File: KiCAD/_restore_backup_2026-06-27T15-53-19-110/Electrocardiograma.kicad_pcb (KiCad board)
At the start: 2 copper layers, 56.5 x 56.9 mm, 63 parts, among them J1 54-00174, J2 Conn_01x02_Pin, J4 Conn_01x02_Pin, J5 Conn_01x02_Pin, J6 Conn_01x04_Pin, U1 INA823DT, U2 ESP32-C3-WROOM-02, U3 TLV1117-33, U4 TLV4888, U5 TLV4888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

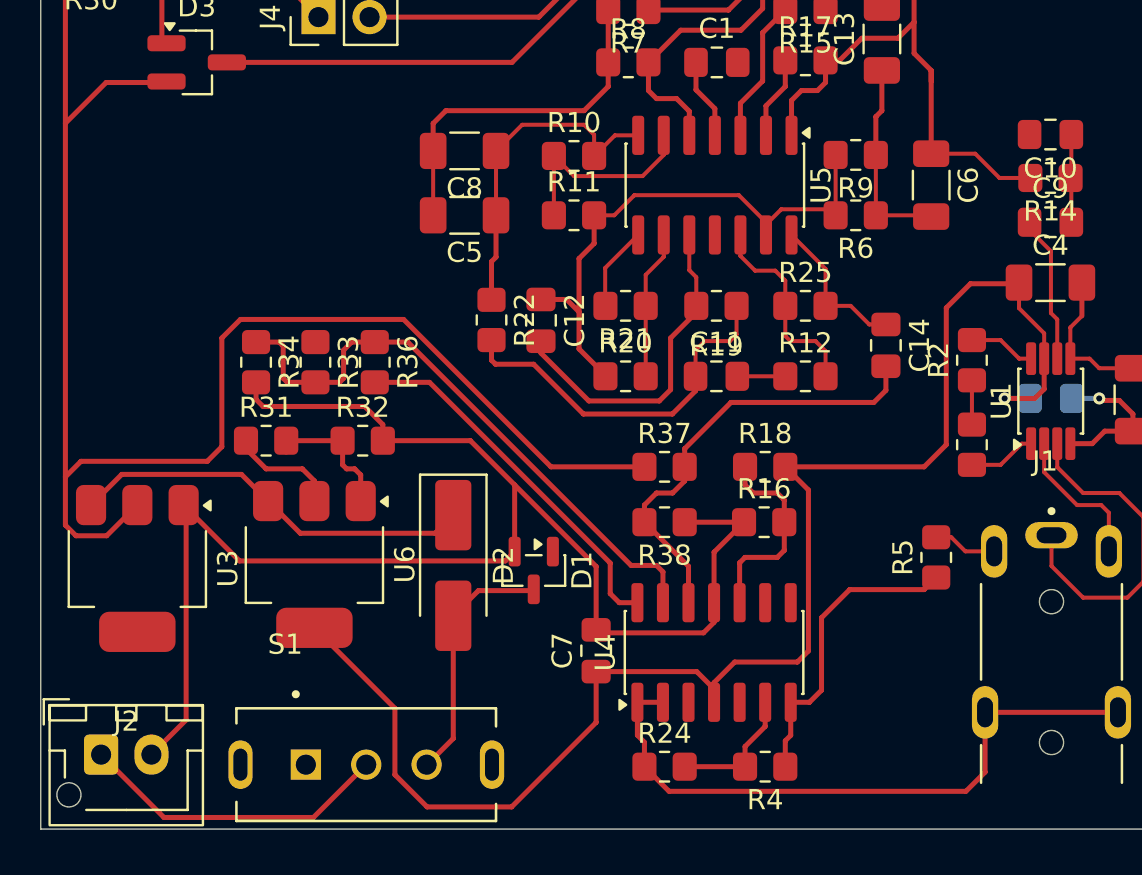
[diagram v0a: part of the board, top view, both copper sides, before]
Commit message: PCB rezise
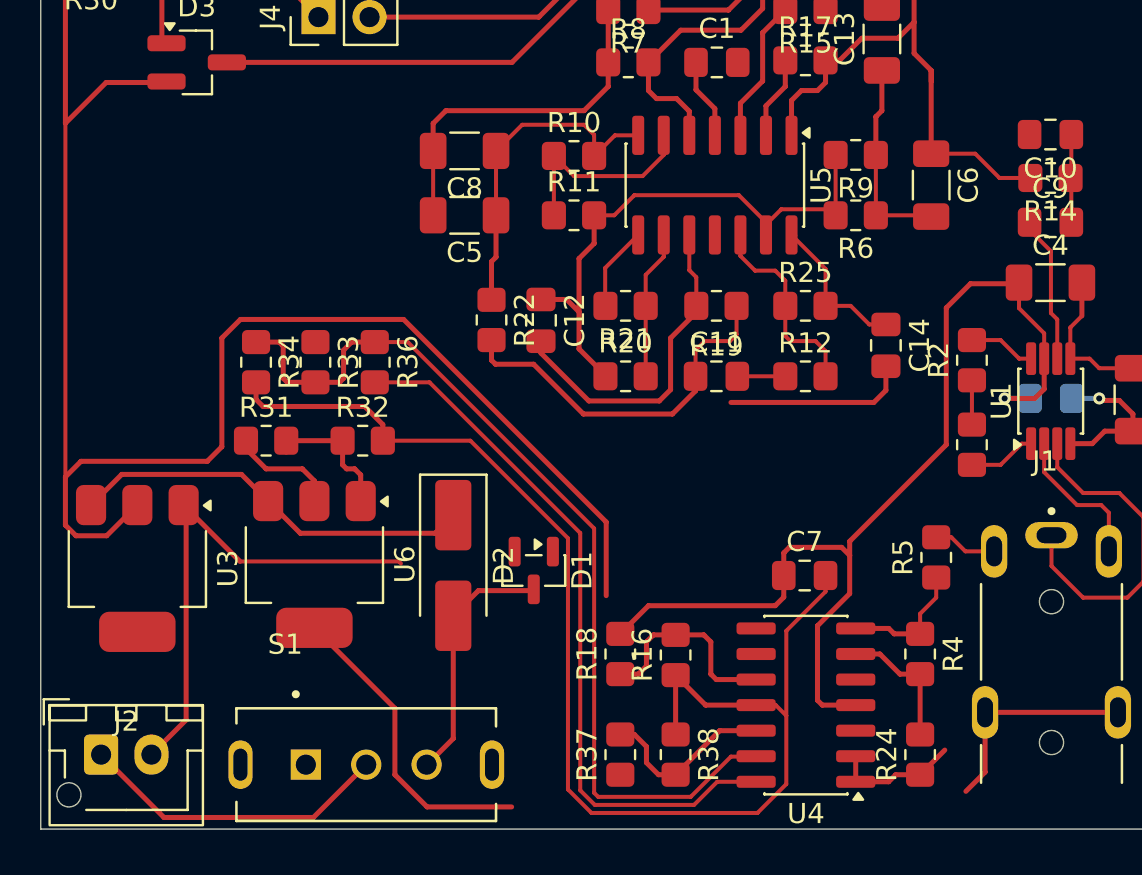
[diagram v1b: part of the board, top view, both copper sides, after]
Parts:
- moved R37 14.5 mm to (153.8, 118.8), turned to 90 degrees
- moved R24 12.7 mm to (168.7, 118.8), turned to 90 degrees
- moved R18 11.8 mm to (153.8, 113.8), turned to 90 degrees
- moved R38 11.6 mm to (156.6, 118.8), turned to -90 degrees
- moved C7 11.0 mm to (163.0, 109.9), turned to 0 degrees
- moved R4 9.52 mm to (168.7, 113.8), turned to -90 degrees
- moved R16 7.93 mm to (156.6, 113.8), turned to 90 degrees
- moved U4 5.26 mm to (163.0, 116.3), turned to 180 degrees
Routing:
- net /Leveled_Signal: track 49.7 -> 66.9 mm
- net Net-(U4D--): track 29.9 -> 46.2 mm
- net -BATT_REG: track 135.9 -> 151.9 mm
- net Net-(U4A--): track 33.4 -> 18.6 mm
- net Net-(R4-Pad1): track 15.2 -> 6.44 mm
- net +6.1V: track 85.6 -> 77.8 mm
- net Net-(U4D-+): track 22.3 -> 18.1 mm
- net +3.3V: track 93.8 -> 96.7 mm
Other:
- board text added: "No conectadas (R_G)"
